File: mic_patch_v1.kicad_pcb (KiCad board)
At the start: 2 copper layers, 30 x 30 mm, 41 parts, among them J1 Conn_ARM_SWD_TagConnect_TC203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, J2 J_000001, J3 J_000001, J4 Micro_SD_Card, SW1 SW_000001, SW2 SW_000001, U1 NORA-B106-00B, U2 PWR_nPM1100-QDXX, U3 ADAU7002ACBZ-R7, Y1 CLK_0003

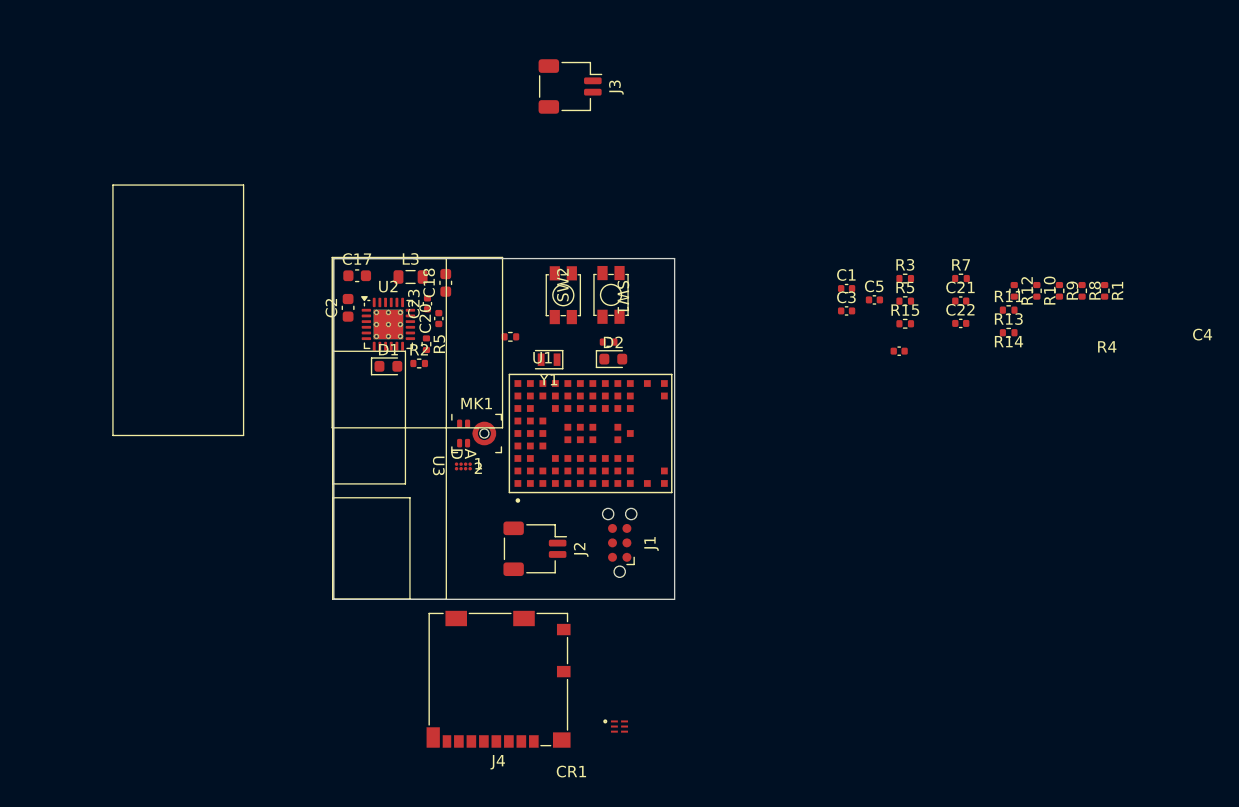
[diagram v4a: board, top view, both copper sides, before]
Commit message: added footprints for every part
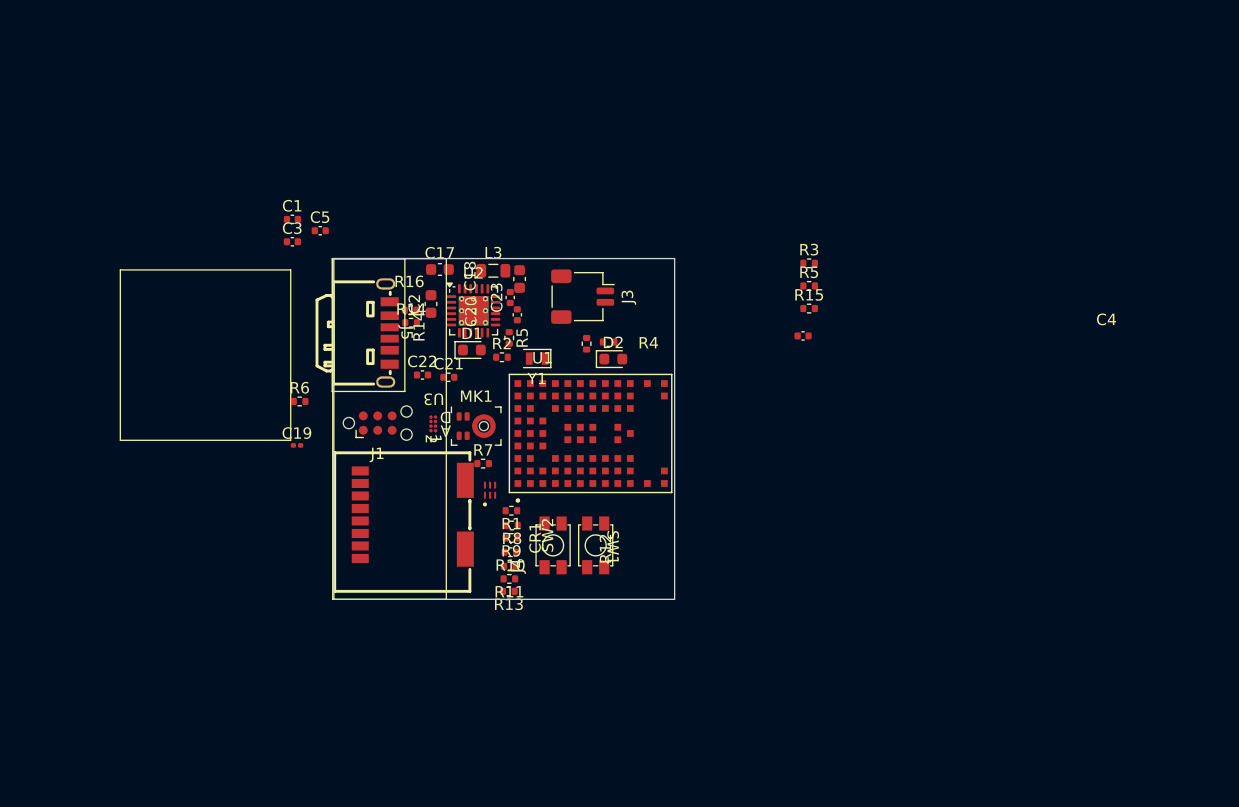
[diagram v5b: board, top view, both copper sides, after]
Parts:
- removed J2: J_000001, mic_patch_parts:J_000001
- added C19: C_00006, Capacitor_SMD:C_0201_0603Metric, F.Cu at (90.5, 77.3)
- added J5: J_000002, mic_patch_parts:C5260493, F.Cu at (98.4, 67.5)
- added R14: R_00006, Resistor_SMD:R_0402_1005Metric, F.Cu at (100.5, 66.5)
- added R16: R_00006, Resistor_SMD:R_0402_1005Metric, F.Cu at (100.5, 65.5)
- added R6: R_00005, Resistor_SMD:R_0402_1005Metric, F.Cu at (90.7, 73.5)
- J4: footprint Connector_Card:microSD_HC_Molex_104031-0811 -> mic_patch_parts:TF-SMD_TF-017
- moved R1 55.7 mm to (109.3, 83.1), turned to 180 degrees
- moved R8 54.3 mm to (109.4, 84.4), turned to 180 degrees
- moved R9 52.9 mm to (109.3, 85.5), turned to 180 degrees
- moved R10 51.7 mm to (109.2, 86.8), turned to 180 degrees
- moved R12 50.6 mm to (109.2, 88.0), turned to 180 degrees
- moved R11 49.9 mm to (109.2, 89.1), turned to 180 degrees
- moved R13 49.6 mm to (109.1, 90.2), turned to 180 degrees
- moved C1 49.2 mm to (90.0, 57.5)
- moved C3 49.2 mm to (90.0, 59.4)
- moved C5 49.2 mm to (92.5, 58.5)
- moved C22 47.6 mm to (101.5, 71.2)
- moved C21 45.6 mm to (103.8, 71.3)
- moved R7 45.1 mm to (106.8, 79.0)
- moved J1 23.8 mm to (97.6, 75.4), turned to 0 degrees
- moved CR1 23.7 mm to (107.5, 81.3), turned to 90 degrees
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
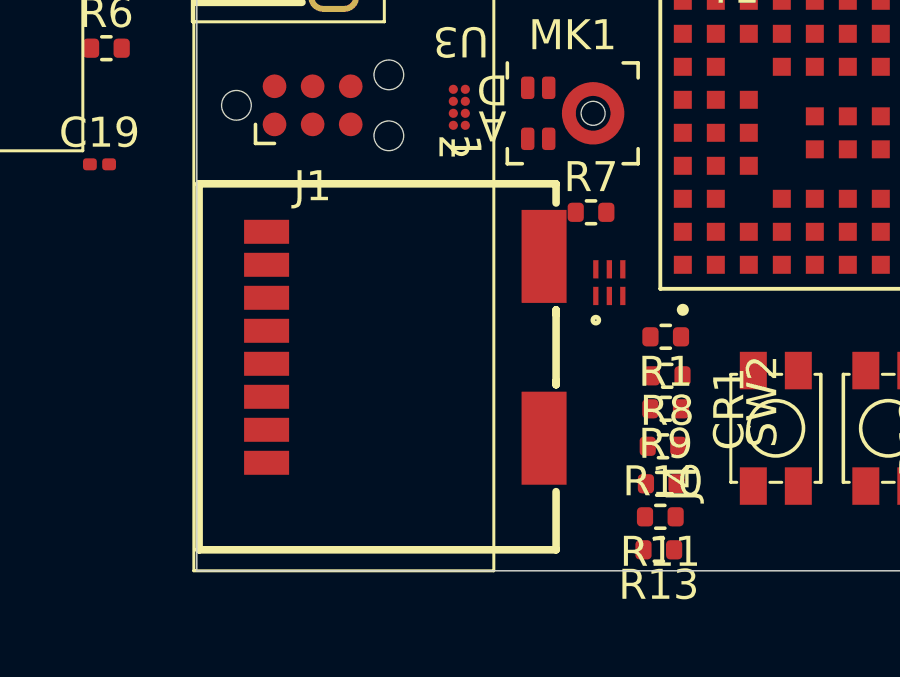
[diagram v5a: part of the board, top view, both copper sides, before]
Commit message: fixed SD card footprintg
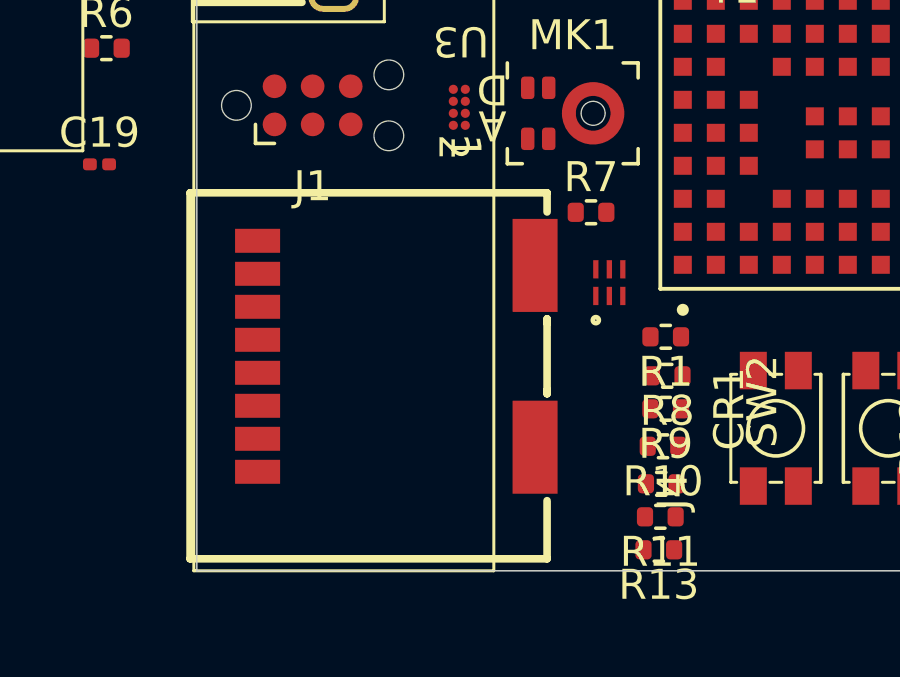
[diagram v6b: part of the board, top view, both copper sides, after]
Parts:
- R14: value R_00002 -> R_00006
- R5: value R_00002 -> R_00004
- moved J4 0.42 mm to (100.3, 83.8)
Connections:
- net Net-(D1-K) renamed /Power/CHG_IND
- net Net-(J1-SWCLK) renamed /MCU/SWCLK
- net Net-(J1-SWDIO) renamed /MCU/SWDIO
- net Net-(MK1-CLOCK) renamed /Mic/PDM_CLK
- net Net-(MK1-L/R) renamed /Mic/L_R
- net Net-(U2-DEC) renamed /Power/DEC_NPM
- net Net-(U2-ICHG) renamed /Power/ICHG
- net Net-(U2-NTC) renamed /Power/NTC
- net Net-(U2-SW) renamed /Power/NPM SW
- net Net-(U2-VBAT) renamed /Power/VBAT
- net Net-(U2-VBUS) renamed /Power/VBUS
- net Net-(U3-PDM_DAT) renamed /Mic/PDM_DAT
- R10 pad 2: Net-(J4-DAT1) -> /SD_card/DAT1_pull_up
- R14 pad 1: Net-(D2-K) -> Net-(J5-CC2)
- R9 pad 2: Net-(J4-DAT2) -> /SD_card/DAT_2_pull_up

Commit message: sketched out power
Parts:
- moved R15 34.3 mm to (103.5, 53.0)
- moved R5 30.6 mm to (109.0, 48.0), turned to 90 degrees
- moved R3 27.8 mm to (109.5, 51.5), turned to 180 degrees
- moved C18 17.3 mm to (108.0, 45.5), turned to 0 degrees
- moved L3 16.8 mm to (104.5, 45.5)
- moved R2 16.6 mm to (109.0, 53.0), turned to 180 degrees
- moved U2 16.0 mm to (105.5, 49.5)
- moved C20 15.9 mm to (109.5, 50.0), turned to 0 degrees
- moved D1 15.0 mm to (105.5, 54.0), turned to -90 degrees
- moved C17 14.7 mm to (101.5, 47.2), turned to 90 degrees
- moved C2 14.4 mm to (101.5, 50.5), turned to -90 degrees
- moved C19 13.8 mm to (101.5, 69.0)
- moved R5 13.6 mm to (107.0, 54.5)
- moved R6 13.1 mm to (103.0, 78.0), turned to 180 degrees
- moved C23 8.95 mm to (107.0, 73.0), turned to 180 degrees
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
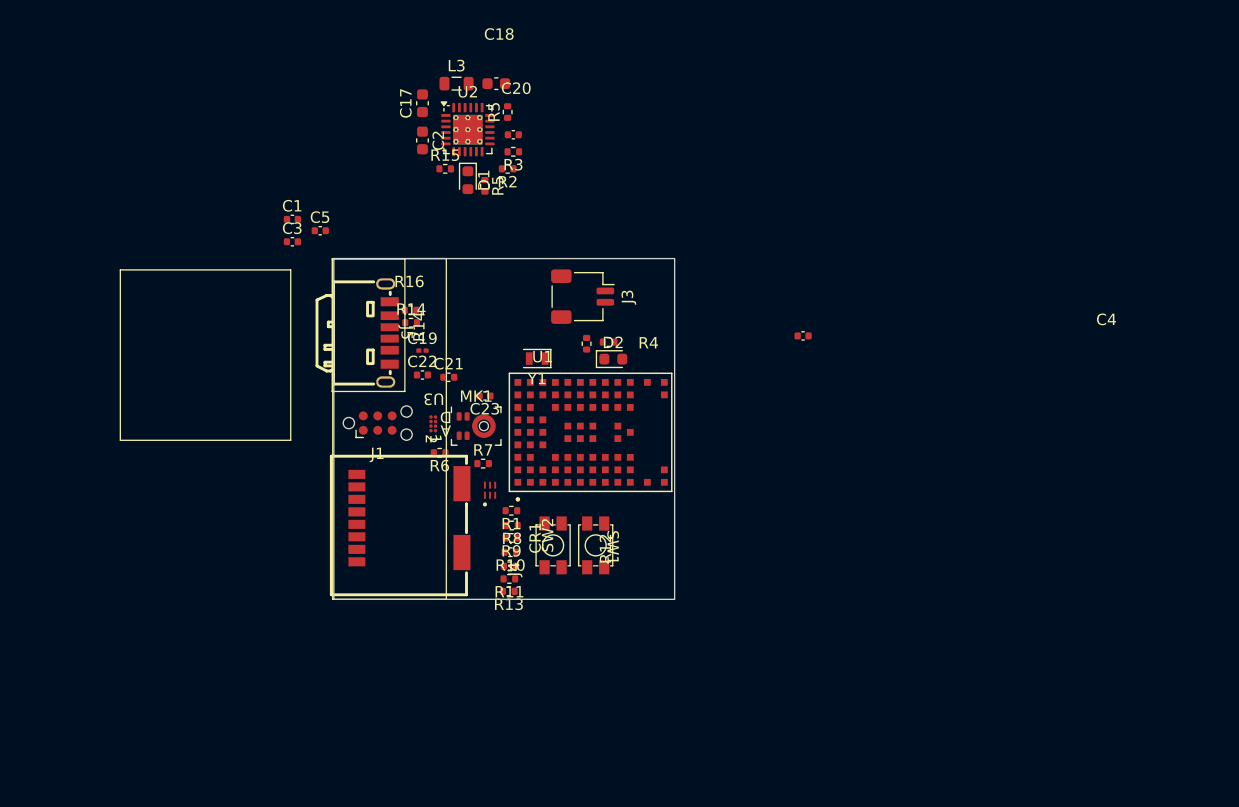
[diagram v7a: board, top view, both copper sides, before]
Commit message: laid out sub modules
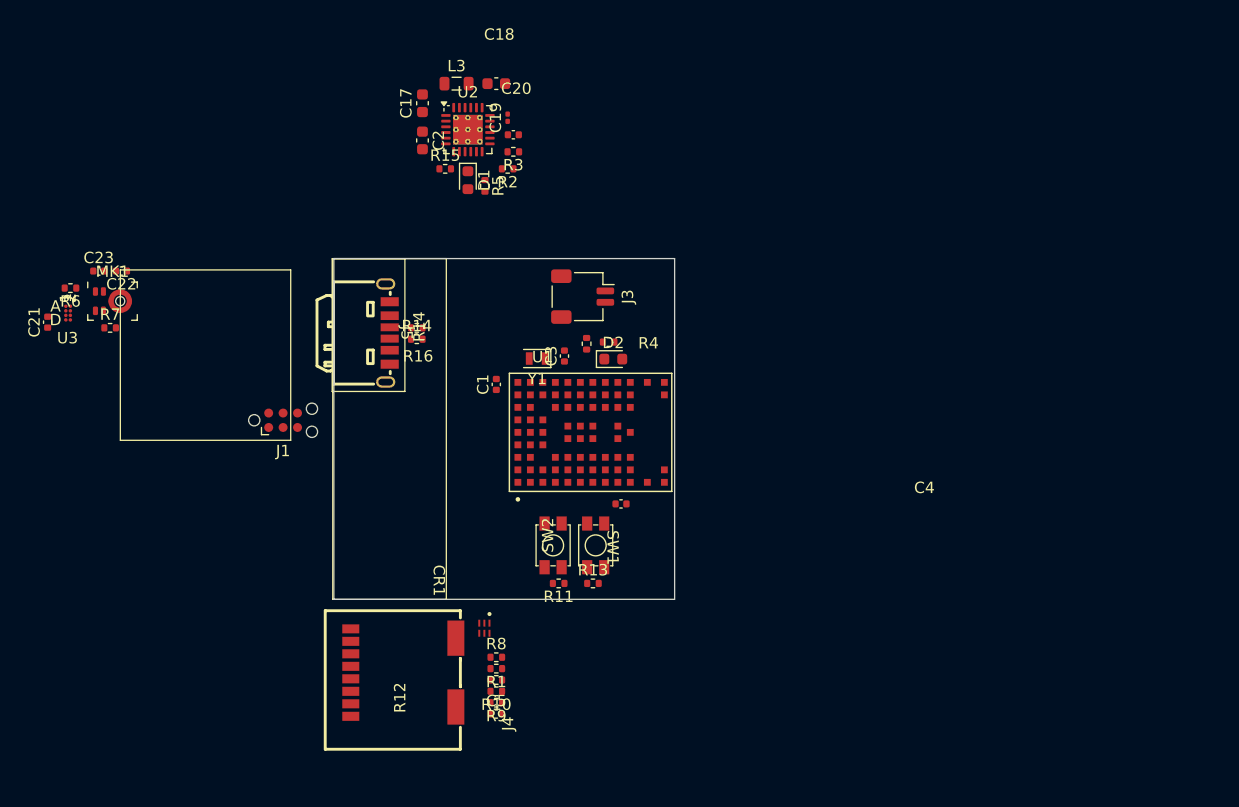
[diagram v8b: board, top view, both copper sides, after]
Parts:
- removed the R5 at (109.0, 48.0)
- moved C5 45.3 mm to (108.0, 101.0)
- moved C23 35.7 mm to (73.0, 62.0), turned to 0 degrees
- moved C21 35.6 mm to (68.5, 66.5), turned to 90 degrees
- moved R6 35.6 mm to (70.5, 63.5)
- moved R7 34.9 mm to (74.0, 67.0)
- moved MK1 33.9 mm to (74.2, 64.7)
- moved U3 33.6 mm to (70.3, 65.7), turned to 0 degrees
- moved C22 28.0 mm to (75.0, 62.0), turned to 180 degrees
- moved C3 26.0 mm to (114.0, 69.5), turned to 90 degrees
- moved C1 23.1 mm to (108.0, 72.0), turned to 90 degrees
- moved C19 21.8 mm to (109.0, 48.5), turned to 90 degrees
- moved C4 21.8 mm to (119.0, 82.5)
- moved R9 14.6 mm to (108.0, 100.0)
- moved R1 14.0 mm to (108.0, 97.0)
- moved J4 13.6 mm to (99.8, 97.3)
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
